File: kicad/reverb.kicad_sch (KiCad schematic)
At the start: 22 parts, among them IC1 TL072CP

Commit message: Datasheet footprints, floor-plan placement, headless autoroute (144/145, DRC 0)
PCB-AUDIT s1 fixes with datasheet-derived project footprints:
- TO-220-5_Vertical_P1.70mm_LM1875 (TI NDH0005D): 1.45 mm pads on the 1.1 mm
  drill -> 0.175 mm annular (was 0.0875, 5 DRC errors); pad-local 0.2 mm clearance
- Bridge_KBP_P3.81mm (Diodes DS39310 KBP404G-KBP410G, pins + ~ ~ -); bridge
  symbol renumbered to the physical order; errata #3 updated (KBU needs a swap)
- value-aware CP/R sizing (real can sizes for 4700/2200/1000 uF, 5 W / 1 W
  resistors, fat pads on the 0R speaker return); Part 4 wire pads for all
  off-board wiring (2.0 mm/1.2 mm signal, 3.0 mm/1.5 mm speaker + transformer)
- VRAW/AC1/AC2 moved into the HighCurrent net class (errata #11)

gen_pcb.py now places to the Part 5 floor plan: balanced columns (Input/Preamp
with Tone stacked below | Reverb/Trem/MRB | Power Amp | PSU), signal order inside
zones with serpentine shelves, LM1875/LM317 on the top edge with the 10 mm
keep-out, wiring edge along the bottom, 4x M3 holes, two locked 0.9 mm escape
stubs off the LM1875 pins 4/5 (a 1.5/2.5 mm trace cannot enter a 1.70 mm pitch).
DRC before routing: 0 errors, 0 warnings.

route_board.py: pcbnew DSN export -> Freerouting -> SES import -> pour refill.
Freerouting 2.1.0 ignores every pass/timeout limit in CLI mode and only writes
output at 0 unrouted (and its MT router crashed), so the script drives 1.9.0
under xvfb-run and injects autoroute_settings (bottom layer 6x cost, via 80) so
the GND pour stays whole. Committed board: 144/145 connections routed, 0 DRC
violations (--severity-all), 26 vias, 351 mm on the bottom vs 3.7 m on top; the
one open PA_OUT link (blocked by R_bias1) is documented as a GUI finish.

Chassis-fit figure corrected: the old 48-53 % / 82-90 % densities counted hidden
text boxes; text-less it is ~33 % on 190x115 and ~56 % on 155x90.

Docs: PCB-NOTES/PCB-AUDIT rewritten, README, CHANGELOG, errata #3/#11,
SOURCES (package drawings), Part 10, kicad RE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
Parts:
- C_rec_byp, C_rev1: footprint Capacitor_THT:CP_Radial_D8.0mm_P3.50mm -> Capacitor_THT:CP_Radial_D5.0mm_P2.00mm
- POT_REV: footprint Connector_PinHeader_2.54mm:PinHeader_1x03_P2.54mm_Vertical -> cambridge_reverb:WirePad_1x03_P2.54mm_D1.2mm
- REV1: footprint Connector_PinHeader_2.54mm:PinHeader_1x04_P2.54mm_Vertical -> cambridge_reverb:WirePad_1x04_P2.54mm_D1.2mm

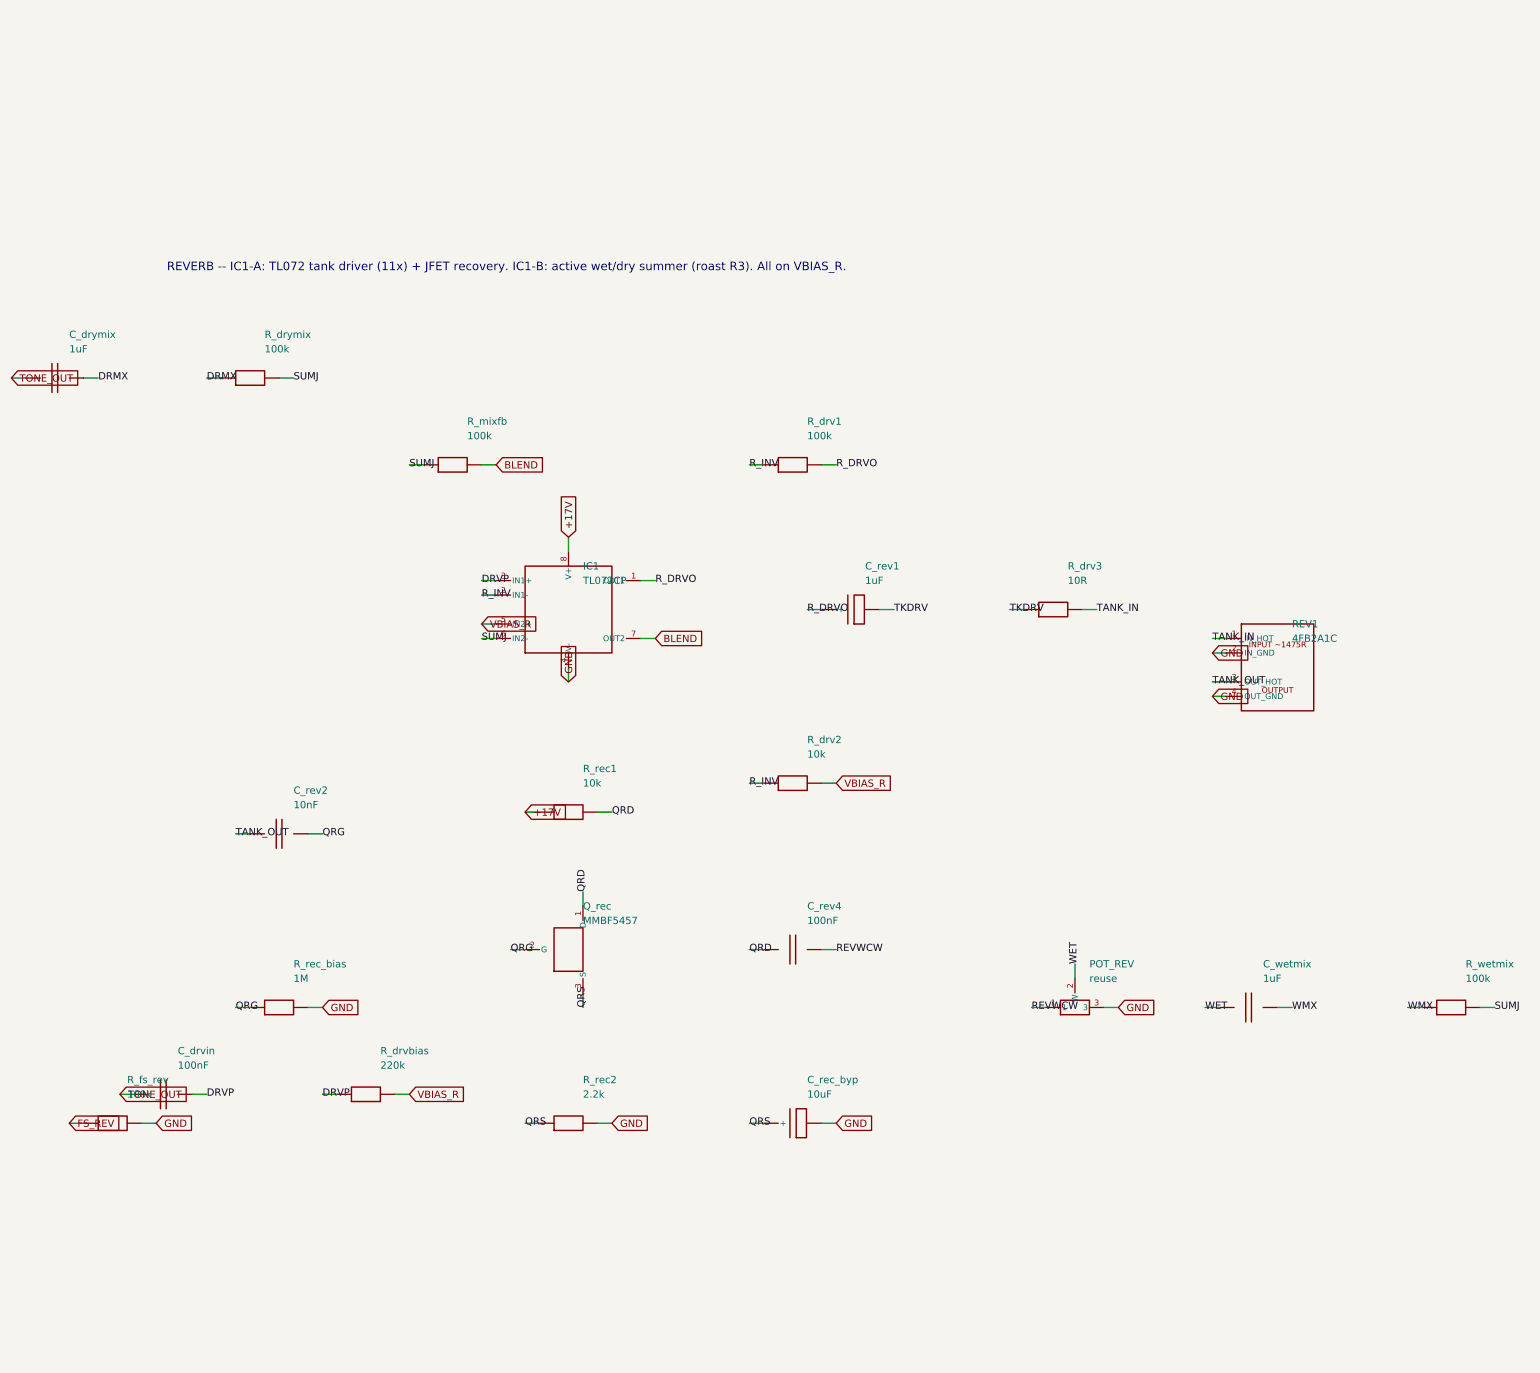
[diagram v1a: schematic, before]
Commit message: Add 26 labelled bench test points (schematic + BOM + silk) and re-route
Test points follow the Part 5 bring-up order: rails (VRAW, +33V5, VREG_IN,
+17V), JFET drains Q1D/Q2D/QRD (the errata #15 bias trim), the VBIAS_R/VBIAS_T
mid-rail refs, every inter-stage node (PREAMP_OUT, TONE_OUT, BLEND, TREM_OUT,
MRB_OUT, PA_IN), tank drive/return, LFO, PA_BIAS/PA_OUT/SPK_P, and a GND pin
per zone for the probe clip.

- gen_kicad.py: one-pin TP symbol; TEST_POINTS table; add_test_points() puts
  them on their sheets so they are in the netlist and the BOM (one order line)
- footprint TestPoint_THT_D2.0mm_Label: 2.0 mm pad / 1.0 mm drill for a header
  pin or wire loop; the footprint VALUE (= net alias) prints on F.SilkS
- gen_pcb.py: test-point strip across the top of each zone; the effects column
  is now two stacked zones (tremolo+MRB above, reverb below next to its tank
  pads) so each block's points sit right above its parts; stacked-zone gap 2 mm
- PCB-NOTES.md: test-point table with expected values (Part 3 troubleshooting,
  Part 2 set-up, ngspice) and the bring-up sequence
- Re-routed (Freerouting 1.9.0, B.Cu x7, via 60): 161/166 connections, 0 DRC
  violations, 54 vias; the five open links are listed for a GUI finish

Co-Authored-By: Claude Fable 5.1 <noreply@anthropic.com>
Claude-Session: https://claude.ai/code/session_01Vk8HkvCugxFpQsBPVnNT2H
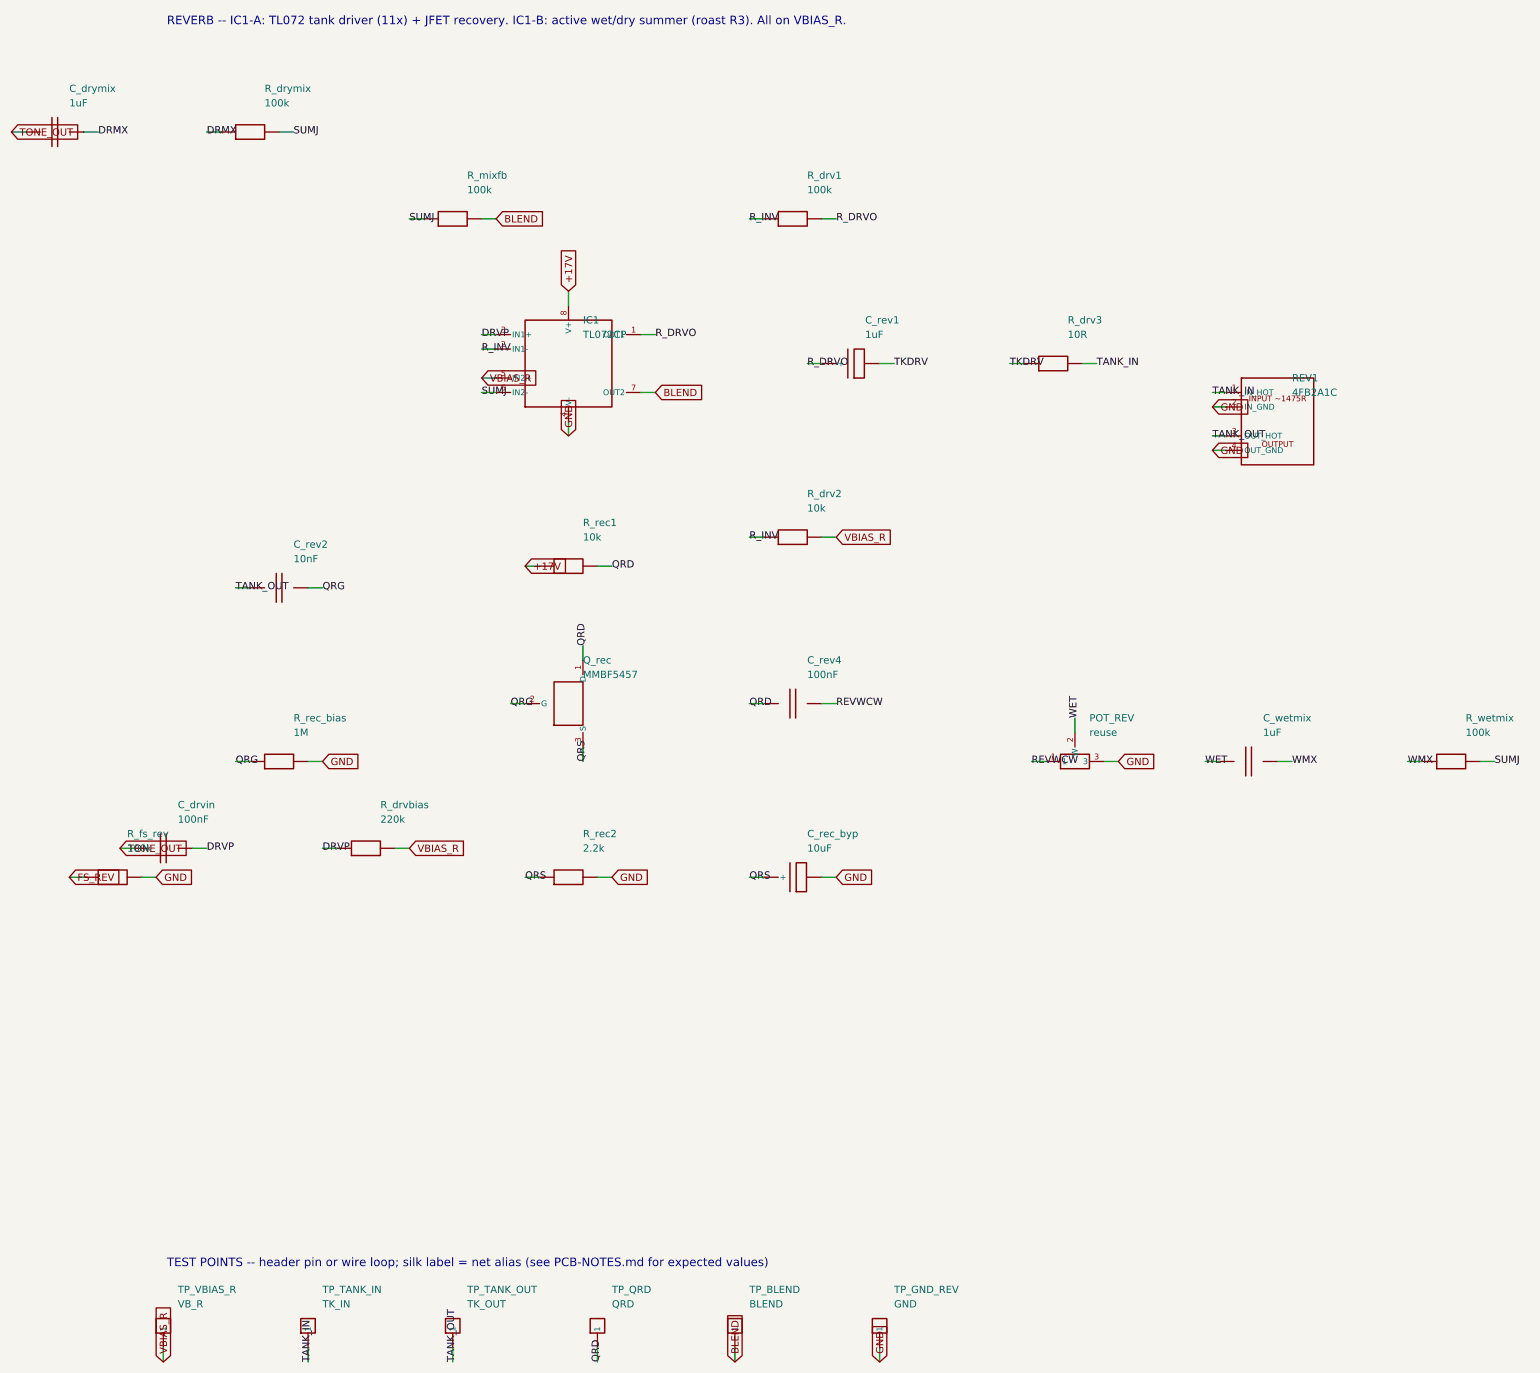
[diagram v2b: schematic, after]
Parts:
- added TP_BLEND: BLEND, cambridge_reverb:TestPoint_THT_D2.0mm_Label, symbol cr_primitives:TP
- added TP_GND_REV: GND, cambridge_reverb:TestPoint_THT_D2.0mm_Label, symbol cr_primitives:TP
- added TP_QRD: QRD, cambridge_reverb:TestPoint_THT_D2.0mm_Label, symbol cr_primitives:TP
- added TP_TANK_IN: TK_IN, cambridge_reverb:TestPoint_THT_D2.0mm_Label, symbol cr_primitives:TP
- added TP_TANK_OUT: TK_OUT, cambridge_reverb:TestPoint_THT_D2.0mm_Label, symbol cr_primitives:TP
- added TP_VBIAS_R: VB_R, cambridge_reverb:TestPoint_THT_D2.0mm_Label, symbol cr_primitives:TP
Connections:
- net BLEND: now also TP_BLEND.1
- net GND: now also TP_GND_REV.1
- net QRD: now also TP_QRD.1
- net TANK_IN: now also TP_TANK_IN.1
- net TANK_OUT: now also TP_TANK_OUT.1
- net VBIAS_R: now also TP_VBIAS_R.1
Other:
- note added: "TEST POINTS -- header pin or wire loop; silk label = net alias (see PCB-NOTES.md for expected values)"

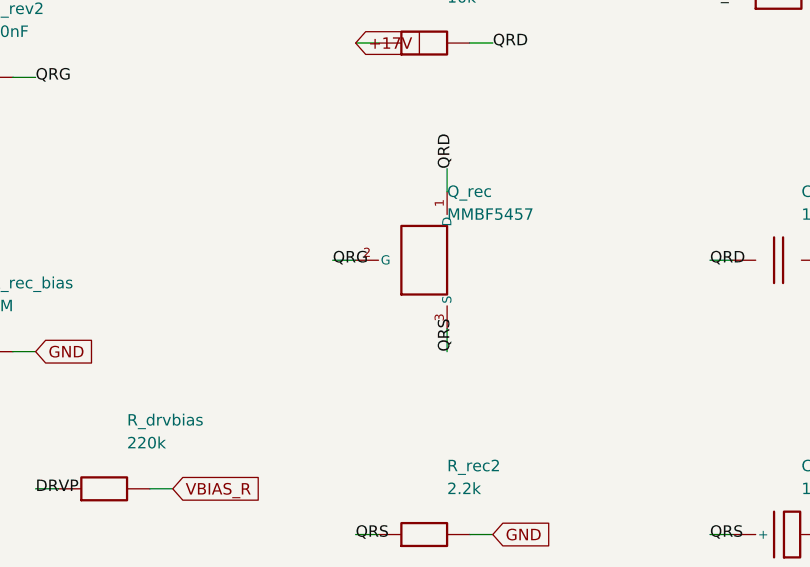
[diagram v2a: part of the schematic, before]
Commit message: Mixed SMD/THT variant (kicad/smd, 155x90), JFET pin-number fix, THT fully routed
Build profiles: gen_kicad.py / gen_pcb.py / gen_bom.py take --profile tht|smd.
One schematic source; the smd profile remaps footprints and writes a self-
contained KiCad project to kicad/smd/ (cambridge_reverb_smd.*, lib tables one
level up), sized 155 x 90 mm for the Part 7 safe-bet chassis.

SMD (70 parts): 0805 R (1206 for R_reg2), 1206 C <= 100 nF, 1210 for 120 nF /
1 uF / C_zobel, SMA + SOD-123 diodes, SOT-23 JFETs fitted directly.
Deliberately THT: power parts, all electrolytics (standing cans use less board
than SMD cans), DIP-8 sockets for the TL072s, the three bench-trimmed JFET
source resistors, LED, connectors, test points. Parts area 4560 mm^2 -> 48 % of
the 155x90 usable area (THT 60 %).

SMD board specifics: 6 mm margin, 0.6 mm gap, 3 mm channels, pad row clear of
the corner holes; GND pour on both layers (top pour solid to SMD ground pads
only, router sees just the bottom plane so every SMD ground pad gets a via);
HighCurrent/Power classes 2.0/1.0 mm for this board (errata #11 addendum).
Routed: 165/167 connections, 1 DRC error (starved thermal), 109 vias; the two
open items are listed in PCB-NOTES as GUI touches. Eight router settings and
three pour strategies compared; the committed one is the best of them.

Errata #18 (HIGH): the JFET symbol had 2 = Gate / 3 = Source; onsemi's 2N5457
(TO-92) and MMBF5457 (SOT-23) both number the leads 1 D / 2 S / 3 G, so the THT
board would have swapped gate and source on Q1, Q2, Q_rec. Symbol renumbered,
both boards regenerated. THT board re-routed (also fixed the column balance):
166/166 connections, 0 DRC violations, 66 vias -- fully routed.

Also: bom/bom-smd*.csv (spec notes, no invented P/Ns), production/smd/
bom-jlcpcb.csv + position file + README for JLCPCB assembly of the SMD side;
route_board.py --drop-planes and default via cost 60; docs (PCB-NOTES,
PCB-AUDIT, README, CHANGELOG, errata, availability audit, Part 10, kicad and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
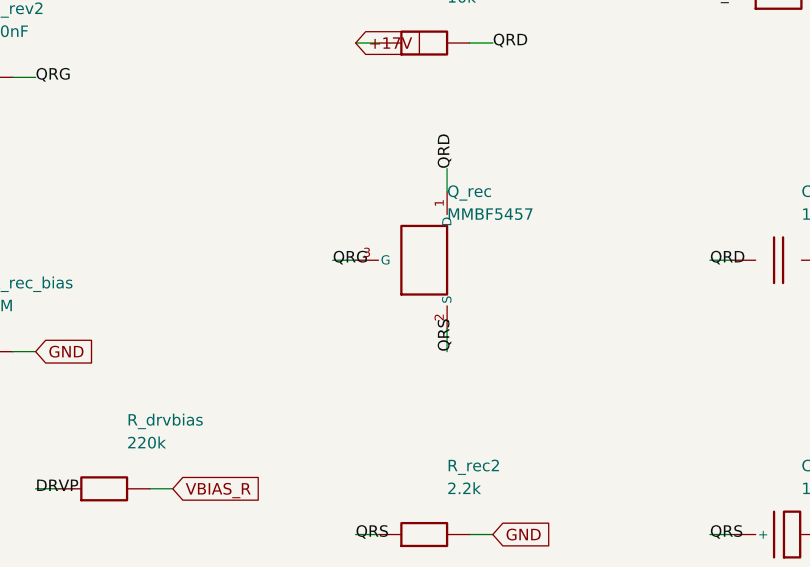
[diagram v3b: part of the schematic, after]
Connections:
- net QRG: now also Q_rec.3 (G); no longer Q_rec.2 (G)
- net QRS: now also Q_rec.2 (S); no longer Q_rec.3 (S)
